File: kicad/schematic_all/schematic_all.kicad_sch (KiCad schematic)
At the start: 42 parts, among them SW1 Button 1, SW2 Encoder 1, SW3 Button 2, SW4 Encoder 2, SW5 Button 3, U1 L7805, U2 RPi_Pico, U3 RDA5807M_Module, U4 LM386

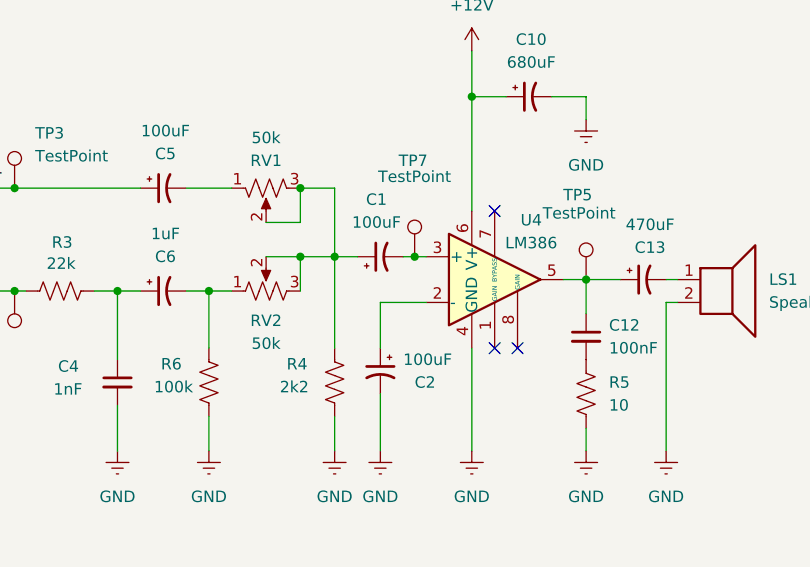
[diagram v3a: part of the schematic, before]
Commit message: unpolarize amp coupling capacitors
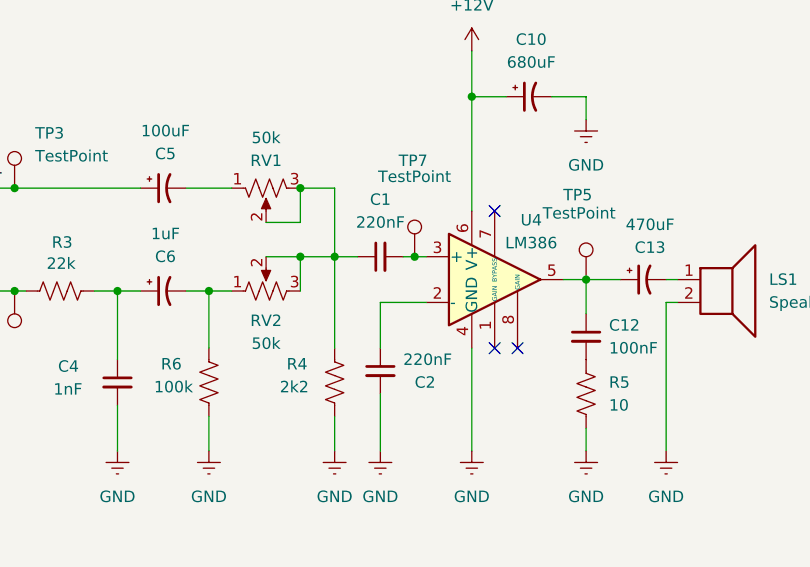
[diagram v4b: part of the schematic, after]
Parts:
- C1, C2: value 100uF -> 220nF; footprint Capacitor_THT:CP_Radial_D5.0mm_P2.00mm -> Capacitor_THT:C_Disc_D5.0mm_W2.5mm_P5.00mm; symbol Device:C_Polarized_Small_US -> Device:C_Small
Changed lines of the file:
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@@
 	)
 	(symbol
-		(lib_id "Device:C_Polarized_Small_US")
+		(lib_id "Device:C_Small")
 		(at 228.6 127 90)
 		(unit 1)
@@
 		(fields_autoplaced yes)
 		(property "Reference" "C1"
-			(at 228.1682 120.65 90)
-			(effects
-				(font
-					(size 1.27 1.27)
-				)
-			)
-		)
-		(property "Value" "100uF"
-			(at 228.1682 123.19 90)
-			(effects
-				(font
-					(size 1.27 1.27)
-				)
-			)
-		)
-		(property "Footprint" "Capacitor_THT:CP_Radial_D5.0mm_P2.00mm"
+			(at 228.6063 120.65 90)
+			(effects
+				(font
+					(size 1.27 1.27)
+				)
+			)
+		)
+		(property "Value" "220nF"
+			(at 228.6063 123.19 90)
+			(effects
+				(font
+					(size 1.27 1.27)
+				)
+			)
+		)
+		(property "Footprint" "Capacitor_THT:C_Disc_D5.0mm_W2.5mm_P5.00mm"
 			(at 228.6 127 0)
 			(effects
@@
 			)
 		)
-		(property "Description" "Polarized capacitor, small US symbol"
+		(property "Description" "Unpolarized capacitor, small symbol"
 			(at 228.6 127 0)
 			(effects
@@
 	)
 	(symbol
-		(lib_id "Device:C_Polarized_Small_US")
+		(lib_id "Device:C_Small")
 		(at 228.6 139.7 0)
 		(mirror y)
@@
 			)
 		)
-		(property "Value" "100uF"
+		(property "Value" "220nF"
 			(at 231.14 138.4365 0)
 			(effects
@@
 			)
 		)
-		(property "Footprint" "Capacitor_THT:CP_Radial_D5.0mm_P2.00mm"
+		(property "Footprint" "Capacitor_THT:C_Disc_D5.0mm_W2.5mm_P5.00mm"
 			(at 228.6 139.7 0)
 			(effects
@@
 			)
 		)
-		(property "Description" "Polarized capacitor, small US symbol"
+		(property "Description" "Unpolarized capacitor, small symbol"
 			(at 228.6 139.7 0)
 			(effects

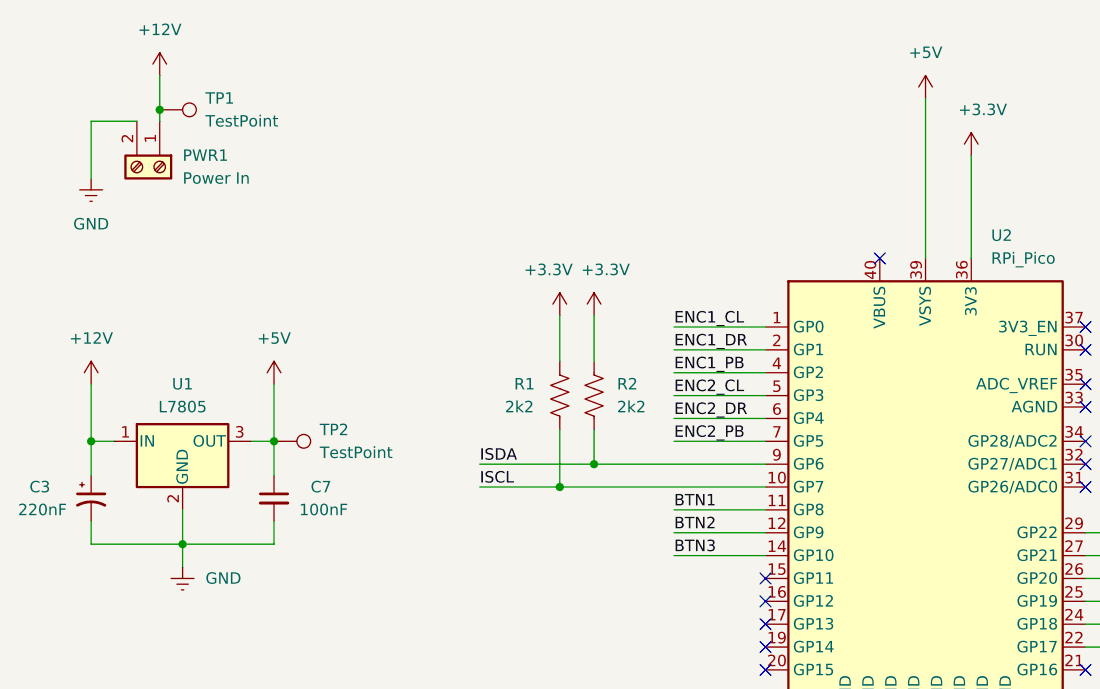
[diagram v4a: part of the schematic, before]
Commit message: fix pico power issues
swap regulator caps to match L4941 spec
add +5V pinout
add diode to prevent backfeeding from pico
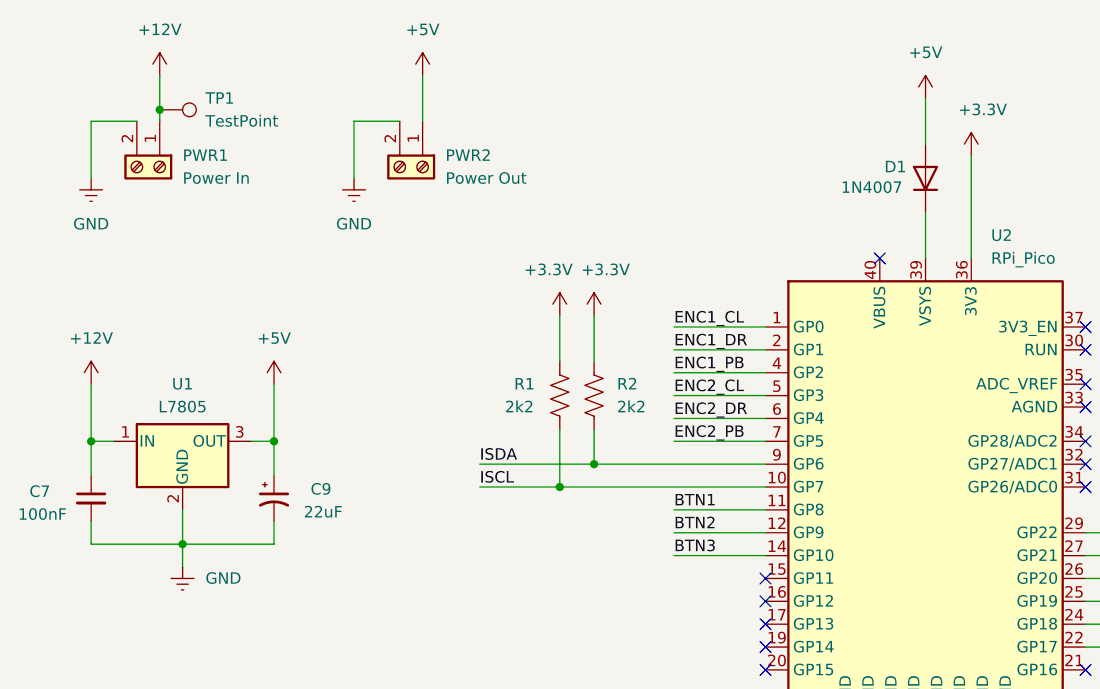
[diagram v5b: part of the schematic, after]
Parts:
- removed C3: 220nF, Capacitor_THT:CP_Radial_D5.0mm_P2.00mm, symbol Device:C_Polarized_Small_US
- removed TP2: TestPoint, Connector_PinHeader_2.54mm:PinHeader_1x01_P2.54mm_Vertical, symbol Connector:TestPoint
- added C9: 22uF, Capacitor_THT:CP_Radial_D5.0mm_P2.00mm, symbol Device:C_Polarized_Small_US
- added D1: 1N4007, Diode_THT:D_DO-41_SOD81_P10.16mm_Horizontal, symbol Device:D
- added PWR2: Power Out, Connector_PinHeader_2.54mm:PinHeader_1x02_P2.54mm_Vertical, symbol Connector:Screw_Terminal_01x02
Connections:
- net +12V: now also C7.1
- net +5V: now also C9.1, D1.2 (A), PWR2.1 (Pin_1); no longer C7.1, U2.39 (VSYS)
- net GND: now also C9.2, PWR2.2 (Pin_2)
- new net: D1.1 (K), U2.39 (VSYS)
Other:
- moved on the sheet: C7

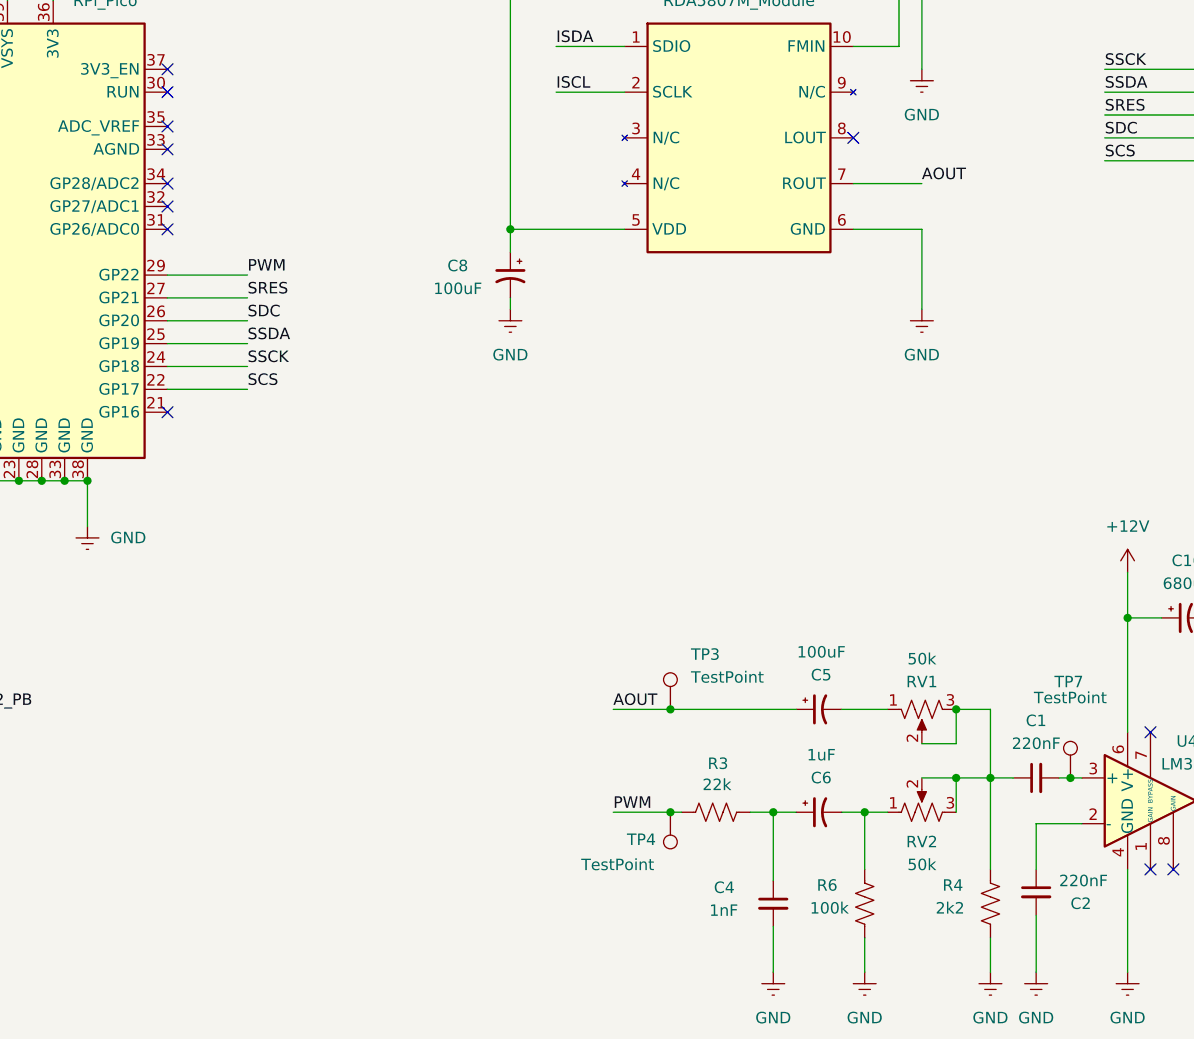
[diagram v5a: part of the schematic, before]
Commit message: add trace and jumper between radio output and pico ADC
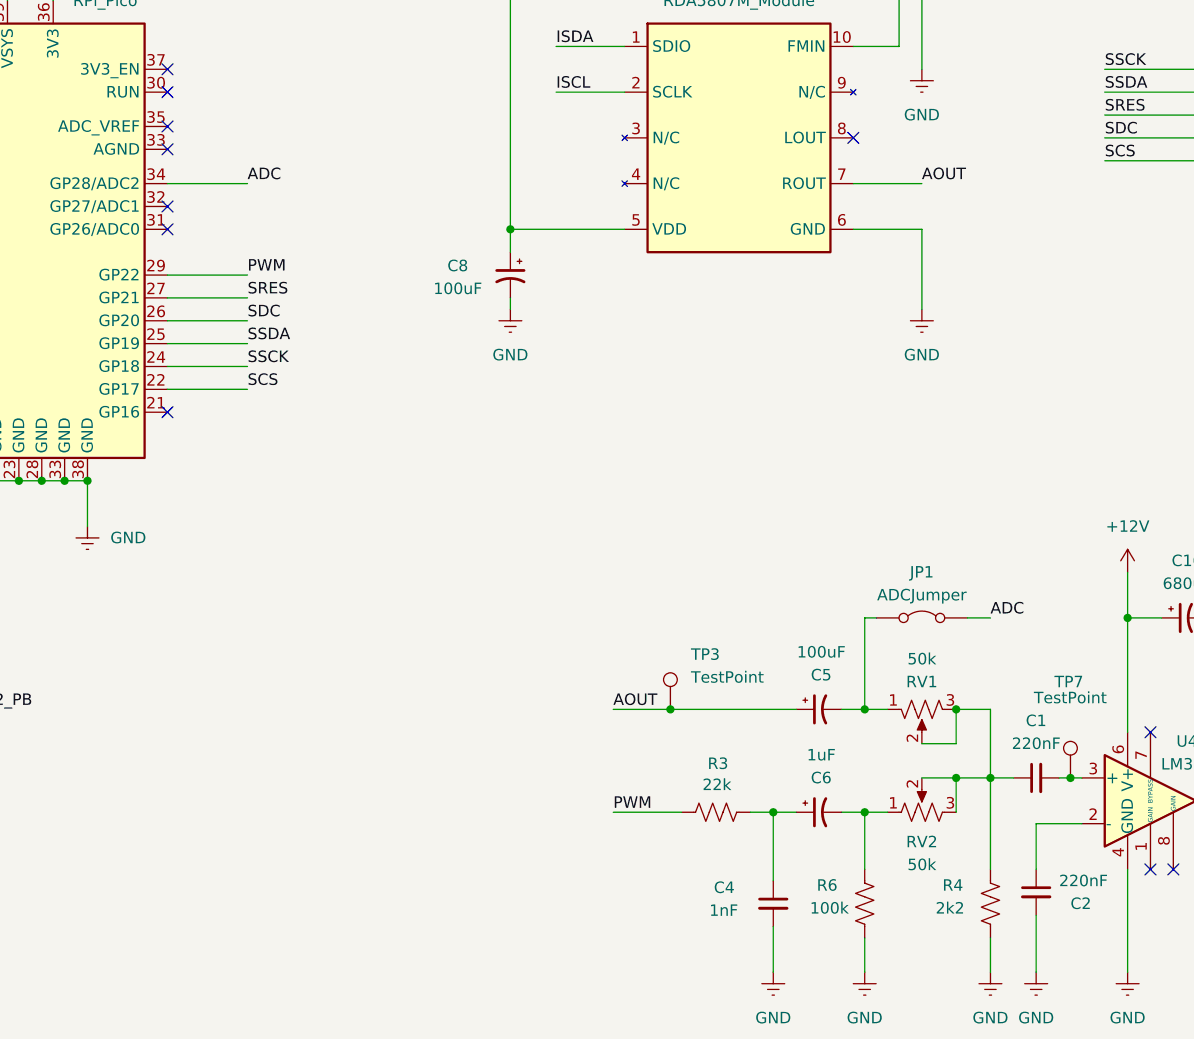
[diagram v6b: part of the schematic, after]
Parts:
- removed TP4: TestPoint, Connector_PinHeader_2.54mm:PinHeader_1x01_P2.54mm_Vertical, symbol Connector:TestPoint
- added JP1: ADCJumper, Connector_PinHeader_2.54mm:PinHeader_1x02_P2.54mm_Vertical, symbol Jumper:Jumper_2_Bridged
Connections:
- net at C5.2, RV1.1: now also JP1.1 (A)
- net ADC: now reaches U2.34 (GP28/ADC2)
- net ADC: now also JP1.2 (B)
- no-connect marks 18 -> 17
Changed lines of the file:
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@@
 	)
 	(junction
-		(at 187.96 130.81)
-		(diameter 0)
-		(color 0 0 0 0)
-	)
-	(junction
 		(at 86.36 121.92)
 		(diameter 0)
@@
 	)
 	(junction
+		(at 209.55 119.38)
+		(diameter 0)
+		(color 0 0 0 0)
+	)
+	(junction
 		(at 29.21 24.13)
 		(diameter 0)
@@
 	)
 	(no_connect
-		(at 132.08 60.96)
-	)
-	(no_connect
 		(at 208.28 55.88)
 	)
@@
 	(wire
 		(pts
+			(xy 220.98 109.22) (xy 223.52 109.22)
+		)
+		(stroke
+			(width 0)
+			(type default)
+		)
+	)
+	(wire
+		(pts
 			(xy 247.65 109.22) (xy 251.46 109.22)
 		)
@@
 	(wire
 		(pts
+			(xy 209.55 109.22) (xy 210.82 109.22)
+		)
+		(stroke
+			(width 0)
+			(type default)
+		)
+	)
+	(wire
+		(pts
 			(xy 102.87 119.38) (xy 109.22 119.38)
 		)
@@
 	(wire
 		(pts
+			(xy 209.55 119.38) (xy 212.09 119.38)
+		)
+		(stroke
+			(width 0)
+			(type default)
+		)
+	)
+	(wire
+		(pts
 			(xy 123.19 93.98) (xy 123.19 99.06)
 		)
@@
 	(wire
 		(pts
-			(xy 181.61 130.81) (xy 187.96 130.81)
-		)
-		(stroke
-			(width 0)
-			(type default)
-		)
-	)
-	(wire
-		(pts
 			(xy 219.71 119.38) (xy 223.52 119.38)
 		)
@@
 	(wire
 		(pts
-			(xy 207.01 119.38) (xy 212.09 119.38)
+			(xy 207.01 119.38) (xy 209.55 119.38)
 		)
 		(stroke
@@
 	(wire
 		(pts
+			(xy 132.08 60.96) (xy 140.97 60.96)
+		)
+		(stroke
+			(width 0)
+			(type default)
+		)
+	)
+	(wire
+		(pts
 			(xy 86.36 50.8) (xy 96.52 50.8)
 		)
@@
 	(wire
 		(pts
-			(xy 187.96 130.81) (xy 189.23 130.81)
+			(xy 181.61 130.81) (xy 189.23 130.81)
 		)
 		(stroke
@@
 		)
 	)
+	(wire
+		(pts
+			(xy 209.55 119.38) (xy 209.55 109.22)
+		)
+		(stroke
+			(width 0)
+			(type default)
+		)
+	)
 	(label "ENC1_PB"
 		(at 59.69 119.38 0)
@@
 		)
 	)
+	(label "ADC"
+		(at 140.97 60.96 0)
+		(fields_autoplaced yes)
+		(effects
+			(font
+				(size 1.27 1.27)
+			)
+			(justify left bottom)
+		)
+	)
 	(label "ENC1_DR"
 		(at 86.36 50.8 0)
@@
 		)
 	)
+	(label "ADC"
+		(at 223.52 109.22 0)
+		(fields_autoplaced yes)
+		(effects
+			(font
+				(size 1.27 1.27)
+			)
+			(justify left bottom)
+		)
+	)
 	(label "ENC1_CL"
 		(at 86.36 48.26 0)
@@
 	)
 	(symbol
+		(lib_id "Jumper:Jumper_2_Bridged")
+		(at 215.9 109.22 0)
+		(unit 1)
+		(exclude_from_sim yes)
+		(in_bom yes)
+		(on_board yes)
+		(dnp no)
+		(fields_autoplaced yes)
+		(property "Reference" "JP1"
+			(at 215.9 104.14 0)
+			(effects
+				(font
+					(size 1.27 1.27)
+				)
+			)
+		)
+		(property "Value" "ADCJumper"
+			(at 215.9 106.68 0)
+			(effects
+				(font
+					(size 1.27 1.27)
+				)
+			)
+		)
+		(property "Footprint" "Connector_PinHeader_2.54mm:PinHeader_1x02_P2.54mm_Vertical"
+			(at 215.9 109.22 0)
+			(effects
+				(font
+					(size 1.27 1.27)
+				)
+				(hide yes)
+			)
+		)
+		(property "Datasheet" "~"
+			(at 215.9 109.22 0)
+			(effects
+				(font
+					(size 1.27 1.27)
+				)
+				(hide yes)
+			)
+		)
+		(property "Description" "Jumper, 2-pole, closed/bridged"
+			(at 215.9 109.22 0)
+			(effects
+				(font
+					(size 1.27 1.27)
+				)
+				(hide yes)
+			)
+		)
+		(pin "1"
+		)
+		(pin "2"
+		)
+		(instances
+			(project ""
+				(path "/017a32bd-a431-4565-87b4-2161296abf15"
+					(reference "JP1")
+					(unit 1)
+				)
+			)
+		)
+	)
+	(symbol
 		(lib_id "power:Earth")
 		(at 215.9 74.93 0)
@@
 					(unit 1)
 				)
-			)
-		)
-	)
-	(symbol
-		(lib_id "Connector:TestPoint")
-		(at 187.96 130.81 180)
-		(unit 1)
-		(exclude_from_sim no)
-		(in_bom yes)
-		(on_board yes)
-		(dnp no)
-		(property "Reference" "TP4"
-			(at 183.134 133.858 0)
-			(effects
-				(font
-					(size 1.27 1.27)
-				)
-				(justify right)
-			)
-		)
-		(property "Value" "TestPoint"
-			(at 178.054 136.652 0)
-			(effects
-				(font
-					(size 1.27 1.27)
-				)
-				(justify right)
-			)
-		)
-		(property "Footprint" "Connector_PinHeader_2.54mm:PinHeader_1x01_P2.54mm_Vertical"
-			(at 182.88 130.81 0)
-			(effects
-				(font
-					(size 1.27 1.27)
-				)
-				(hide yes)
-			)
-		)
-		(property "Datasheet" "~"
-			(at 182.88 130.81 0)
-			(effects
-				(font
-					(size 1.27 1.27)
-				)
-				(hide yes)
-			)
-		)
-		(property "Description" "test point"
-			(at 187.96 130.81 0)
-			(effects
-				(font
-					(size 1.27 1.27)
-				)
-				(hide yes)
-			)
-		)
-		(pin "1"
-		)
-		(instances
-			(project "schematic_all"
-				(path "/017a32bd-a431-4565-87b4-2161296abf15"
-					(reference "TP4")
-					(unit 1)
-				)
